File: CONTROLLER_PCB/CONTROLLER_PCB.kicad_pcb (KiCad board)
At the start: 2 copper layers, 114 parts, among them J1 10103594-0001LF, J10 Conn_01x01, J2 Barrel_Jack, J3 Conn_02x07_Odd_Even, J4 Conn_01x04, J5 Conn_01x06, J6 Conn_01x03, J7 Conn_01x03, J8 Conn_01x01, J9 Conn_01x01, Q1 Q_PMOS_GDS, Q2 Q_NMOS_GSD, Q3 Q_NMOS_GSD, Q4 Q_PMOS_GDS, Q5 Q_NMOS_GSD, Q6 Q_NMOS_GSD, Q7 Q_NPN_BEC, Q8 Q_NPN_BEC, Q9 Q_NPN_BEC, U1 AZ1117CH-3_3TRG1, U2 TS462CDT, U3 TPS55340PWP, U4 ESP32-WROOM, Y1 32.768 kHz

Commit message: Updated placement...
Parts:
- moved C24 213.8 mm to (284.2, 106.7)
- moved C27 202.1 mm to (250.5, 73.7)
- moved R3 192.0 mm to (1.44, 190.5)
- moved C26 189.9 mm to (235.3, 66.0)
- moved R5 189.6 mm to (2.37, 195.6)
- moved R4 188.2 mm to (2.37, 185.4)
- moved C25 187.5 mm to (234.9, 63.5)
- moved L2 185.1 mm to (6.35, 132.1), turned to 90 degrees
- moved R13 184.4 mm to (16.3, 85.1)
- moved R12 184.0 mm to (13.8, 91.4)
- moved R7 180.4 mm to (8.89, 196.8)
- moved R10 178.3 mm to (87.6, 25.4)
- moved R11 177.4 mm to (87.5, 21.6)
- moved R16 174.5 mm to (30.3, 91.4)
- moved C23 173.8 mm to (231.1, 72.4), turned to 270 degrees
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
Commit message: Updated BOM & added PCB shape to layout... this is right before removing power supply components...
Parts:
- moved R1 250.2 mm to (252.3, 188.3), turned to 90 degrees
- moved R3 246.9 mm to (248.4, 189.5)
- moved R5 246.2 mm to (248.4, 186.9)
- moved R4 241.3 mm to (243.6, 189.5), turned to 180 degrees
- moved U2 236.0 mm to (245.4, 181.2)
- moved R7 234.8 mm to (243.5, 186.9)
- moved C8 225.5 mm to (240.9, 179.3), turned to 270 degrees
- moved R8 215.7 mm to (237.3, 183.8)
- moved D7 212.0 mm to (247.9, 171.7), turned to 90 degrees
- moved C13 211.8 mm to (213.0, 167.3)
- moved C16 211.8 mm to (226.9, 174.9)
- moved C17 211.8 mm to (219.3, 167.3)
- moved R9 211.8 mm to (228.4, 178.9)
- moved U3 211.8 mm to (226.2, 167.0)
- moved C11 211.8 mm to (216.8, 167.3)
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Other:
- board outline added: 70 x 50 mm

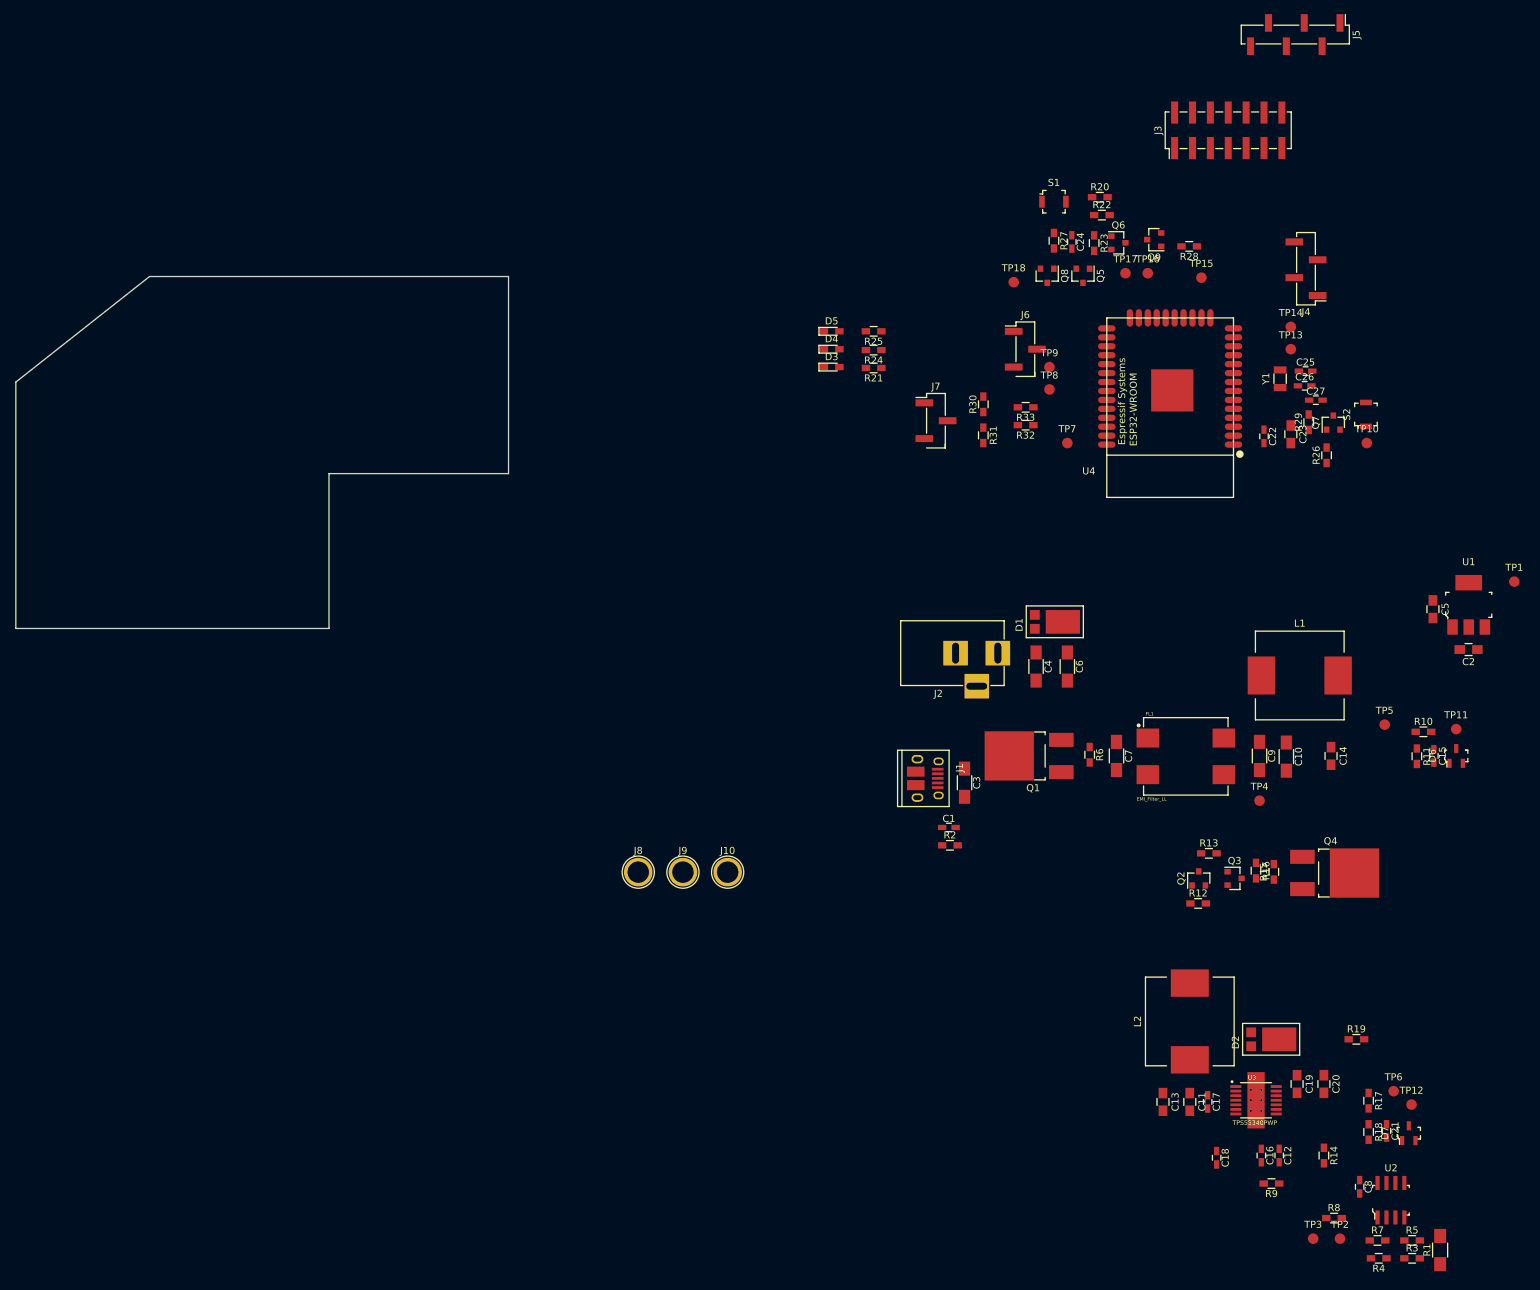
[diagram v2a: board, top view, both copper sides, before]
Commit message: Updated POWER_PCB & CONTROLLER_PCB sch's and layouts
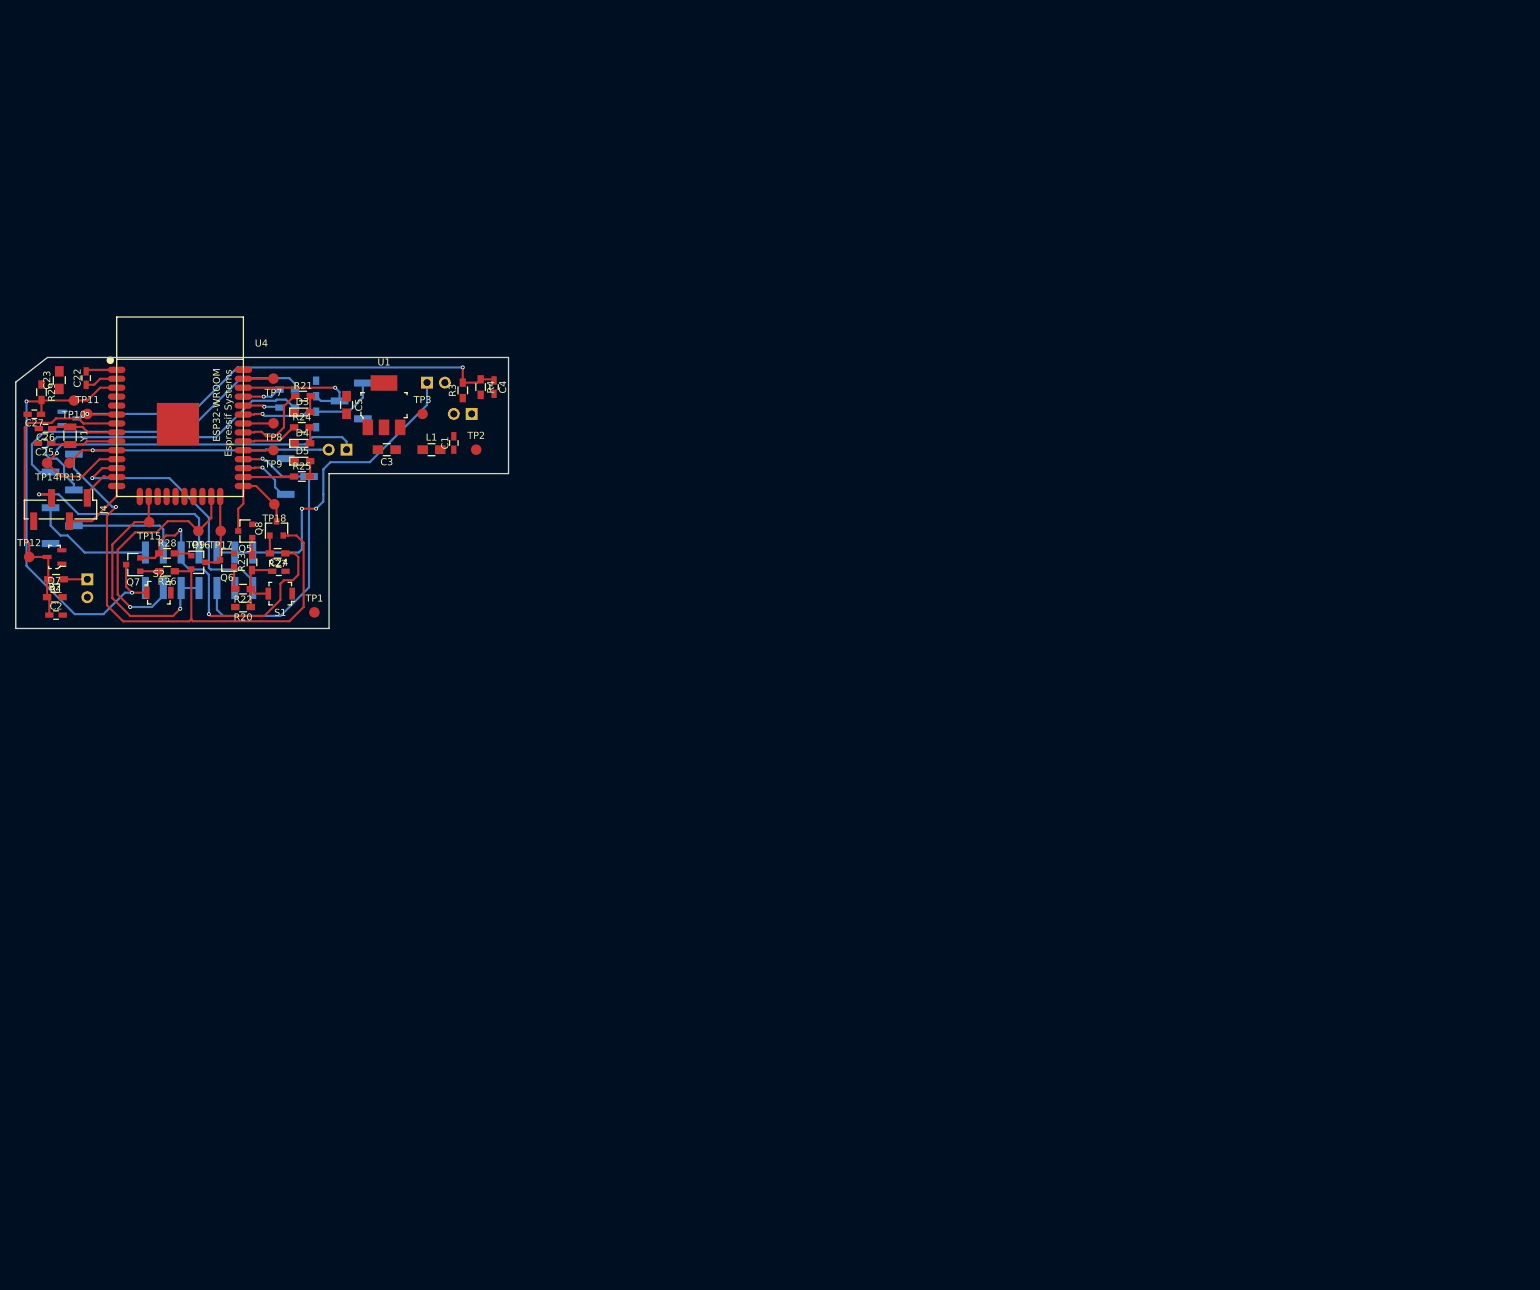
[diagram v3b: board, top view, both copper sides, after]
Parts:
- removed C10, C6, C7, C9: 22uF, Capacitors_SMD:C_1206_HandSoldering
- removed C11, C13, C14, C19, C20: 10uF, Capacitors_SMD:C_0805_HandSoldering
- removed C12, C17, C8: 0.1uF, Capacitors_SMD:C_0603_HandSoldering
- removed C15, C18, C21: 0.01uF, Capacitors_SMD:C_0603_HandSoldering
- removed C16: 100p, Capacitors_SMD:C_0603_HandSoldering
- removed D1, D2: D_Schottky_AKA, PowerDI5:Diodes_Incorporated_POWERDI_5
- removed FL1: EMI_Filter_LL, CustomFootprints:IND_ACM12V-701-2PL-TL00_FixedPadNumbers
- removed J10: Conn_01x01, Connectors:1pin
- removed L2: 10uH, CustomFootprints:L_12x12mm_h8mm_hand_soldering
- removed Q1, Q4: Q_PMOS_GDS, TO_SOT_Packages_SMD:TO-252-2_Rectifier
- removed Q2, Q3: Q_NMOS_GSD, TO_SOT_Packages_SMD:SOT-23
- removed R10, R12, R15, R17, R7: 10k, Resistors_SMD:R_0603_HandSoldering
- removed R11: 2.49k, Resistors_SMD:R_0603_HandSoldering
- removed R13, R18, R5: 1k, Resistors_SMD:R_0603_HandSoldering
- removed R14: 30k, Resistors_SMD:R_0603_HandSoldering
- removed R16, R19: 0 OHM, Resistors_SMD:R_0603_HandSoldering
- removed R6: 20k, Resistors_SMD:R_0603_HandSoldering
- removed R8: 100 OHM, Resistors_SMD:R_0603_HandSoldering
- removed R9: 2.2k, Resistors_SMD:R_0603_HandSoldering
- removed TP4, TP5, TP6: TEST, Measurement_Points:Measurement_Point_Round-SMD-Pad_Small
- removed U2: TS462CDT, digikey-footprints:SOIC-8_W3.9mm
- removed U3: TPS55340PWP, CustomFootprints:SOP65P640X120-15N_HAND_SOLDERING
- C1: value 100p -> 0.1uF
- C2: value 10uF -> 0.1uF; footprint Capacitors_SMD:C_0805_HandSoldering -> Capacitors_SMD:C_0603_HandSoldering
- C3: value 22uF -> 10uF; footprint Capacitors_SMD:C_1206_HandSoldering -> Capacitors_SMD:C_0805_HandSoldering
- C4: value 22uF -> 0.1uF; footprint Capacitors_SMD:C_1206_HandSoldering -> Capacitors_SMD:C_0603_HandSoldering
- D6, J3, J5, J6, J7, R30, R31, R32, R33: moved to B.Cu
- J1: value 10103594-0001LF -> Conn_01x02; footprint Connectors:USB_Micro-B_10103594-0001LF -> Pin_Headers:Pin_Header_Straight_1x02_Pitch2.54mm; moved to B.Cu
- J2: value Barrel_Jack -> Conn_01x02; footprint Connectors:BARREL_JACK -> Pin_Headers:Pin_Header_Straight_1x02_Pitch2.54mm; moved to B.Cu
- J8, J9: value Conn_01x01 -> Conn_01x02; footprint Connectors:1pin -> Pin_Headers:Pin_Header_Straight_1x02_Pitch2.54mm; moved to B.Cu
- L1: value 1uH -> Ferrite_Bead; footprint CustomFootprints:L_12x12mm_h8mm_hand_soldering -> Capacitors_SMD:C_0805_HandSoldering
- R1: value 0.25 OHM -> 10k; footprint Resistors_SMD:R_1206_HandSoldering -> Resistors_SMD:R_0603_HandSoldering
- R2: value 1M -> 1k
- R3: value 1k -> 10k
- R4: value 10k -> 2.49k
- moved R1 218.5 mm to (55.7, 93.0), turned to 180 degrees
- moved TP12 211.2 mm to (51.9, 89.8)
- moved D7 209.1 mm to (55.5, 89.8), turned to 180 degrees
- moved D6 202.8 mm to (57.6, 70.2), turned to 0 degrees
- moved C2 200.7 mm to (55.7, 98.1), turned to 0 degrees
- moved TP11 199.6 mm to (60.2, 69.5)
- moved J5 187.2 mm to (56.6, 81.6), turned to 180 degrees
- moved TP10 183.8 mm to (58.3, 67.6), turned to 180 degrees
- moved R3 182.7 mm to (113.5, 66.2), turned to 90 degrees
- moved C27 182.1 mm to (52.6, 69.6), turned to 180 degrees
- moved J4 180.2 mm to (56.4, 83.1), turned to 270 degrees
- moved R29 180.1 mm to (53.6, 66.4), turned to 270 degrees
- moved C25 179.4 mm to (54.1, 73.7), turned to 180 degrees
- moved C26 179.0 mm to (54.2, 71.6), turned to 180 degrees
- moved R4 177.8 mm to (116.0, 65.7), turned to 270 degrees
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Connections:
- C1 pad 1: Net-(C1-Pad1) -> Vin
- C1 pad 2: Net-(C1-Pad2) -> GND
- C2 pad 1: Vin -> ADC_VOUT
- C3 pad 2: Net-(C1-Pad2) -> GND
- C4 pad 1: Net-(C4-Pad1) -> ADC_VIN
- C4 pad 2: Net-(C1-Pad2) -> GND
- J1 pad 1: Net-(C3-Pad1) -> Vin
- J1 pad 2: Net-(J1-Pad2) -> GND
- J2 pad 1: Net-(C4-Pad1) -> Net-(J2-Pad1)
- J2 pad 2: Net-(C1-Pad2) -> GND
- J8 pad 1: Net-(J8-Pad1) -> DOUT
- J9 pad 1: LED_RTN -> BOOST_BYPASS
- L1 pad 1: Net-(C10-Pad1) -> Net-(C3-Pad1)
- R1 pad 1: LED_RTN -> Net-(J2-Pad1)
- R1 pad 2: GND -> ADC_VOUT
- R2 pad 1: Net-(C1-Pad1) -> ADC_VOUT
- R2 pad 2: Net-(C1-Pad2) -> GND
- R3 pad 1: Net-(R3-Pad1) -> Vin
- R3 pad 2: LED_RTN -> ADC_VIN
- R4 pad 1: Net-(R3-Pad1) -> ADC_VIN
- TP1 pad 1: +3V3 -> GND
- TP2 pad 1: Net-(R7-Pad1) -> Vin
- TP3 pad 1: Net-(R8-Pad1) -> +3V3
- U1 pad 3: Vin -> Net-(C3-Pad1)
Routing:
- net ~DTR: track 0.00 -> 76.8 mm, vias 0 -> 1
- net ADC_VIN: track 0.00 -> 68.9 mm, vias 0 -> 2
- net ~RST: track 0.00 -> 64.6 mm, vias 0 -> 2
- net BOOST_BYPASS: track 0.00 -> 57.5 mm, vias 0 -> 1
- net TXDO: track 0.00 -> 48.4 mm
- net DOUT: track 0.00 -> 47.8 mm, vias 0 -> 2
- net RXDI: track 0.00 -> 46.8 mm
- net U2TXD: track 0.00 -> 44.4 mm, vias 0 -> 1
- net ~RTS: track 0.00 -> 44.2 mm, vias 0 -> 2
- net ADC_VOUT: track 0.00 -> 43.6 mm
- net BOOST_EN: track 0.00 -> 41.1 mm, vias 0 -> 1
- net DO_0: track 0.00 -> 38.1 mm, vias 0 -> 1
- net IO15: track 0.00 -> 34.9 mm, vias 0 -> 1
- net IO13: track 0.00 -> 34.5 mm, vias 0 -> 1
- net SPI_MOSI: track 0.00 -> 31.0 mm, vias 0 -> 1
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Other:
- board size 70 x 50 mm -> 70 x 38.5 mm
- net class Default: clearance 0.2 -> 0.1524; trace_width 0.25 -> 0.3048; via_dia 0.6 -> 0.5588; via_drill 0.4 -> 0.3048
- rule trace_clearance: 0.2 -> 0.1524
- rule trace_min: 0.2 -> 0.1524
- rule via_min_drill: 0.3 -> 0.254
- rule via_min_size: 0.4 -> 0.508

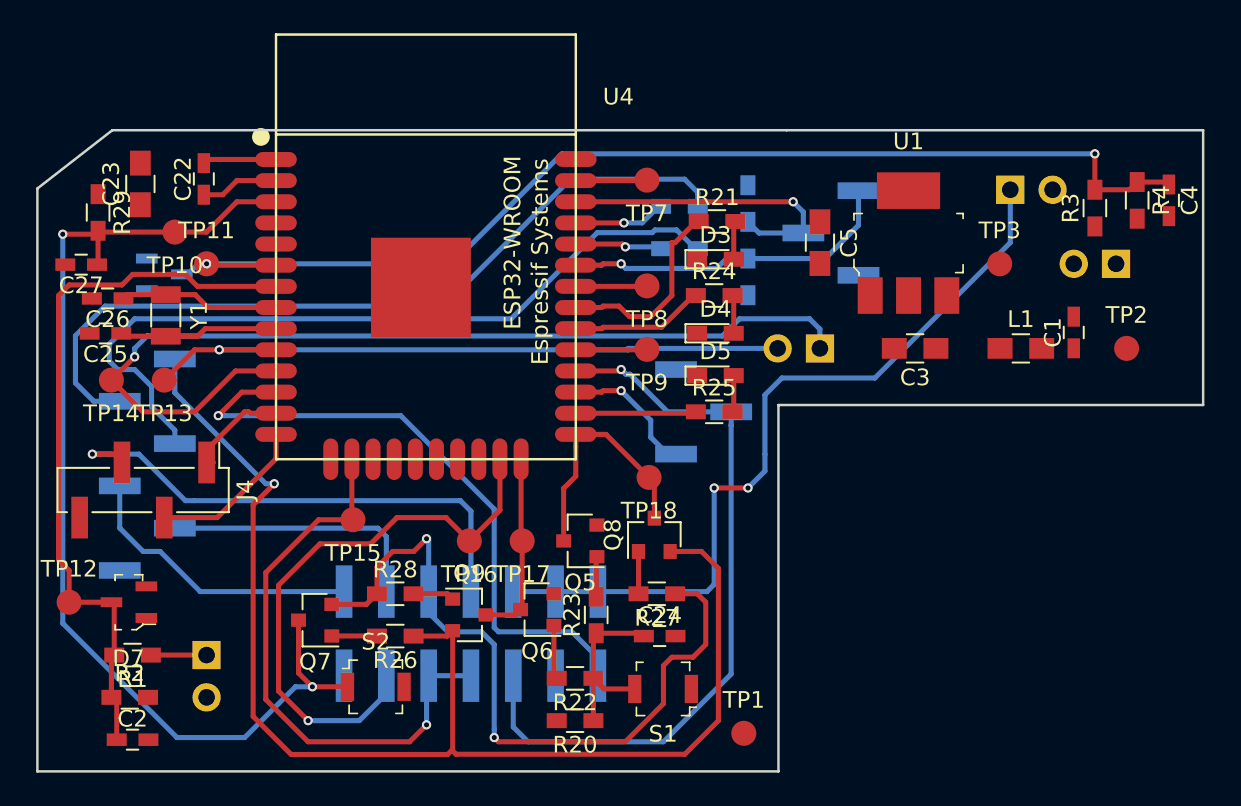
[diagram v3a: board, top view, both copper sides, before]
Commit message: Finished controller layout, and 80% done with power PCB layout.
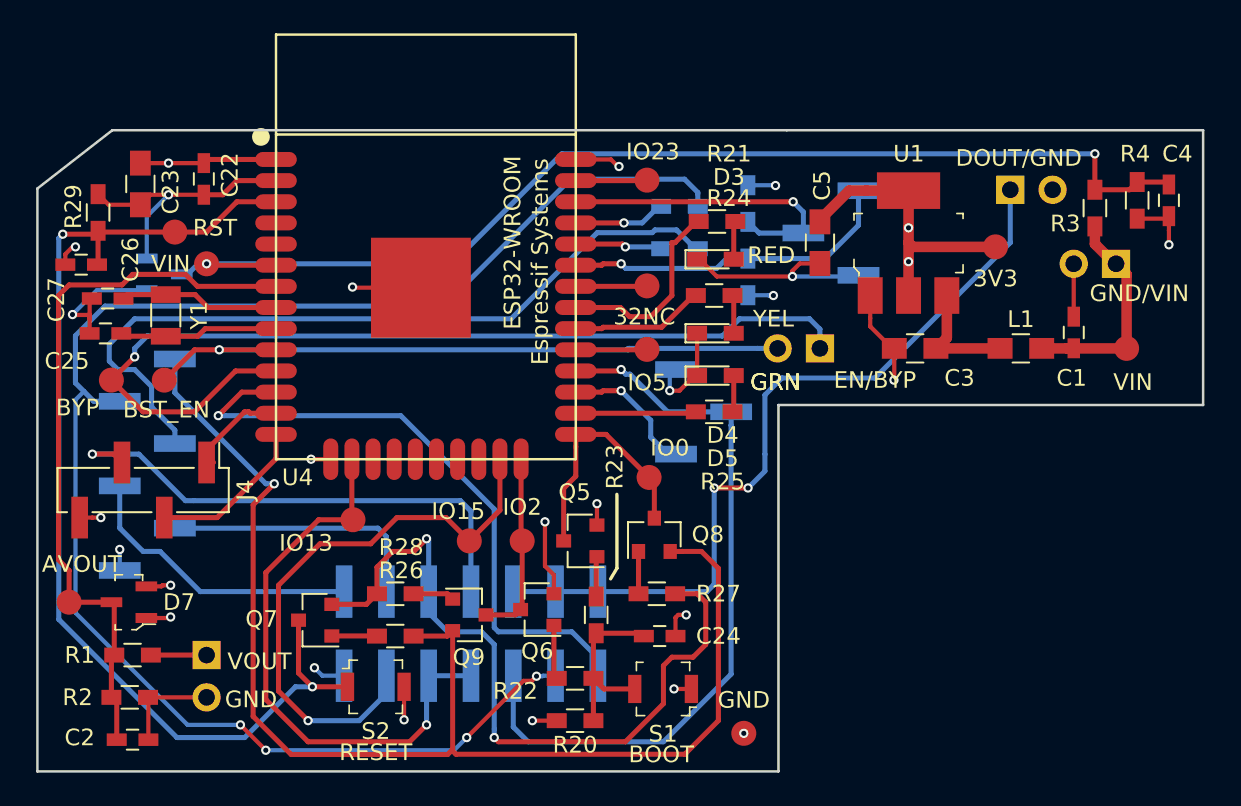
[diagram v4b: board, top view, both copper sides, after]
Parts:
- moved 3V3 1.05 mm to (107.5, 68.5)
- renumbered TP8 to 32NC, TP3 to 3V3, TP12 to AVOUT, TP13 to BST_EN, TP14 to BYP, TP1 to GND, TP18 to IO0, TP15 to IO13, TP16 to IO15, TP17 to IO2, TP7 to IO23, TP9 to IO5, TP11 to RST, TP2 to VIN, TP10 to VIN
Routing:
- net GND: track 4.43 -> 78.3 mm, vias 0 -> 19
- net TXDO: track 48.4 -> 96.0 mm, vias 0 -> 4
- net +3V3: track 4.69 -> 41.4 mm, vias 0 -> 8
- net Vin: track 0.00 -> 13.6 mm
- net Net-(C3-Pad1): track 0.00 -> 7.31 mm
- added copper zone on In2.Cu, net +3V3
- added copper zone on In1.Cu, net GND
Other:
- copper layers 2 -> 4
- board text added: "BOOT"
- board text added: "CONTROLLER_PCB Rev01"
- board text added: "DOUT/GND"
- board text added: "EN/BYP"
- board text added: "GND"
- board text added: "GND/VIN"
- board text added: "GRN"
- board text added: "RED"
- board text added: "RESET"
- board text added: "VOUT"
- board text added: "YEL"
